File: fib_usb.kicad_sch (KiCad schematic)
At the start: 137 parts, among them J401 USB-C_USB4105-GF-A, J402 Conn_USB-C_WE_632723300011, U402 TPS65988DHRSHR, U403 FT230X_QFN, U404 AP22615A_TSOT26, U405 TUSB1046-DCIRNQ, U406 AP22615A_TSOT26, U407 TPD4E05U06QDQARQ1, U408 TPD4E05U06QDQARQ1, U409 W25Q80DV_USON, U410 TPD4E05U06QDQARQ1, U411 TPD4E05U06QDQARQ1, U412 TPD4E05U06QDQARQ1

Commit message: added some missing footprints, stared working ono power-on and sequencing
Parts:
- U403: footprint jetson-orin-baseboard-footprints:QFN-16-1EP_4x4mm_P0.65mm -> Fibel2:QFN-16_1EP_4x4mm_P0.65mm
- U404, U406: footprint jetson-orin-baseboard-footprints:TSOT23-6 -> Fibel2:TSOT23-6
- U405: footprint jetson-orin-baseboard-footprints:WQFN-40_1EP_6x3mm_Pitch0.4mm_EP4.7x2.7mm -> Fibel2:WQFN-40_1EP_6x3mm_Pitch0.4mm_EP4.7x2.7mm
- U407, U408, U410, U411, U412: footprint jetson-orin-baseboard-footprints:USON-10_2.5x1mm_P0.5mm -> Fibel2:USON-10_2.5x1mm_P0.5mm
- U409: footprint jetson-orin-baseboard-footprints:USON-8_2x3mm_P0.5mm -> Fibel2:USON-8_2x3mm_P0.5mm
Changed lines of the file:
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@@
 			)
 		)
-		(property "Footprint" "jetson-orin-baseboard-footprints:USON-10_2.5x1mm_P0.5mm"
+		(property "Footprint" "Fibel2:USON-10_2.5x1mm_P0.5mm"
 			(at 321.31 160.02 0)
 			(effects
@@
 			)
 		)
-		(property "Footprint" "jetson-orin-baseboard-footprints:TSOT23-6"
+		(property "Footprint" "Fibel2:TSOT23-6"
 			(at 144.78 210.82 0)
 			(effects
@@
 			)
 		)
-		(property "Footprint" "jetson-orin-baseboard-footprints:USON-10_2.5x1mm_P0.5mm"
+		(property "Footprint" "Fibel2:USON-10_2.5x1mm_P0.5mm"
 			(at 346.71 160.02 0)
 			(effects
@@
 			)
 		)
-		(property "Footprint" "jetson-orin-baseboard-footprints:USON-10_2.5x1mm_P0.5mm"
+		(property "Footprint" "Fibel2:USON-10_2.5x1mm_P0.5mm"
 			(at 364.49 220.98 0)
 			(effects
@@
 			)
 		)
-		(property "Footprint" "jetson-orin-baseboard-footprints:USON-10_2.5x1mm_P0.5mm"
+		(property "Footprint" "Fibel2:USON-10_2.5x1mm_P0.5mm"
 			(at 358.14 40.64 0)
 			(effects
@@
 			)
 		)
-		(property "Footprint" "jetson-orin-baseboard-footprints:QFN-16-1EP_4x4mm_P0.65mm"
+		(property "Footprint" "Fibel2:QFN-16_1EP_4x4mm_P0.65mm"
 			(at 96.52 163.83 0)
 			(effects
@@
 			)
 		)
-		(property "Footprint" "jetson-orin-baseboard-footprints:TSOT23-6"
+		(property "Footprint" "Fibel2:TSOT23-6"
 			(at 292.1 55.88 0)
 			(effects
@@
 			)
 		)
-		(property "Footprint" "jetson-orin-baseboard-footprints:USON-10_2.5x1mm_P0.5mm"
+		(property "Footprint" "Fibel2:USON-10_2.5x1mm_P0.5mm"
 			(at 297.18 160.02 0)
 			(effects
@@
 			)
 		)
-		(property "Footprint" "jetson-orin-baseboard-footprints:USON-8_2x3mm_P0.5mm"
+		(property "Footprint" "Fibel2:USON-8_2x3mm_P0.5mm"
 			(at 368.3 185.42 0)
 			(effects
@@
 			)
 		)
-		(property "Footprint" "jetson-orin-baseboard-footprints:WQFN-40_1EP_6x3mm_Pitch0.4mm_EP4.7x2.7mm"
+		(property "Footprint" "Fibel2:WQFN-40_1EP_6x3mm_Pitch0.4mm_EP4.7x2.7mm"
 			(at 251.46 106.68 0)
 			(effects

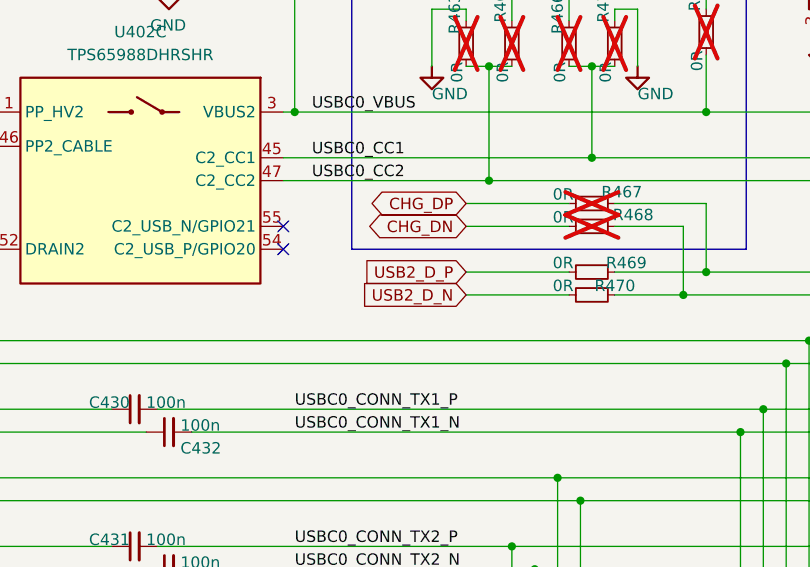
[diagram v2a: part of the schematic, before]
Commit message: started routing the SODIMM, updated connector footprint, started arranging component into sub-areas
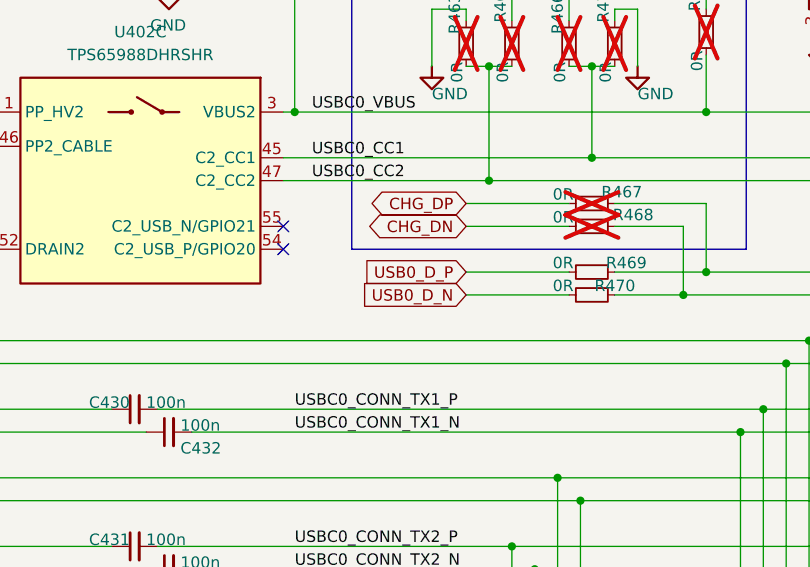
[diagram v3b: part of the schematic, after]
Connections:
- net USB2_D_N renamed USB0_D_N
- net USB2_D_P renamed USB0_D_P
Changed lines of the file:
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@@
 		)
 	)
-	(global_label "USB2_D_N"
+	(global_label "USB0_D_N"
 		(shape input)
 		(at 313.69 93.98 180)
@@
 		)
 	)
-	(global_label "USB2_D_P"
+	(global_label "USB0_D_P"
 		(shape input)
 		(at 313.69 91.44 180)

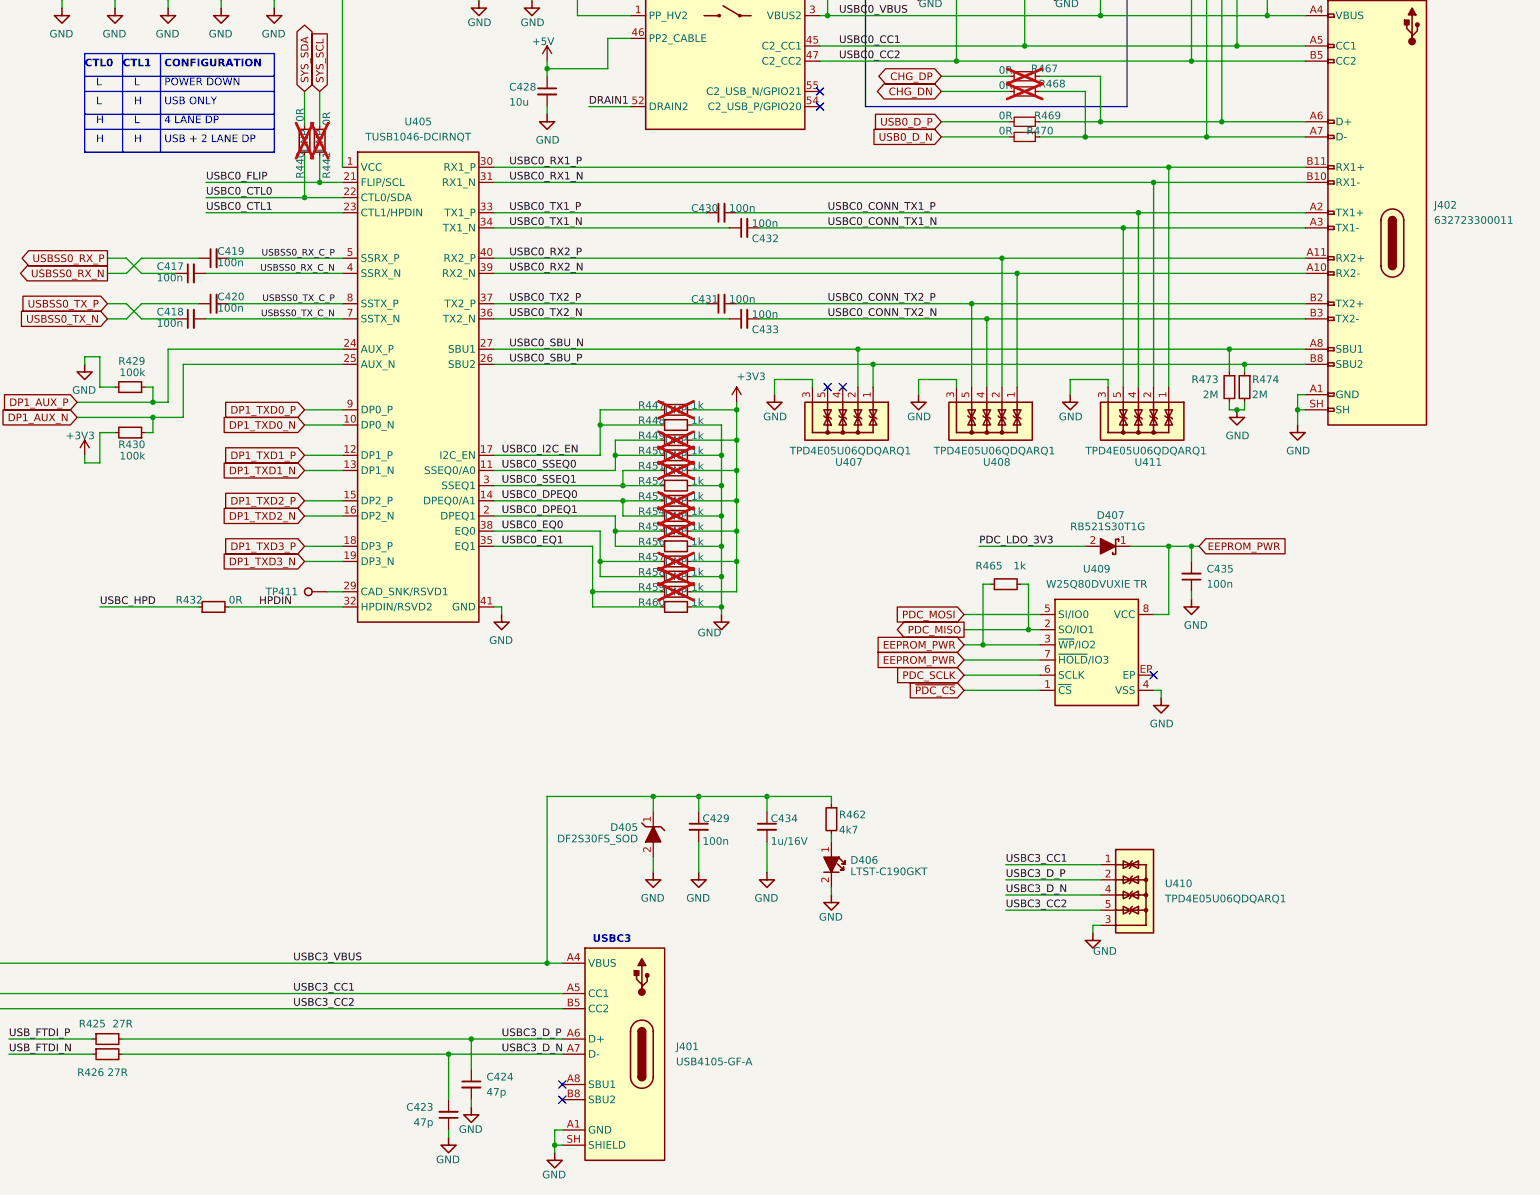
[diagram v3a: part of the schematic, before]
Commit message: did a ton of routing and modeling for SOM, USB, DP & Charging/Power, things starting to take shape
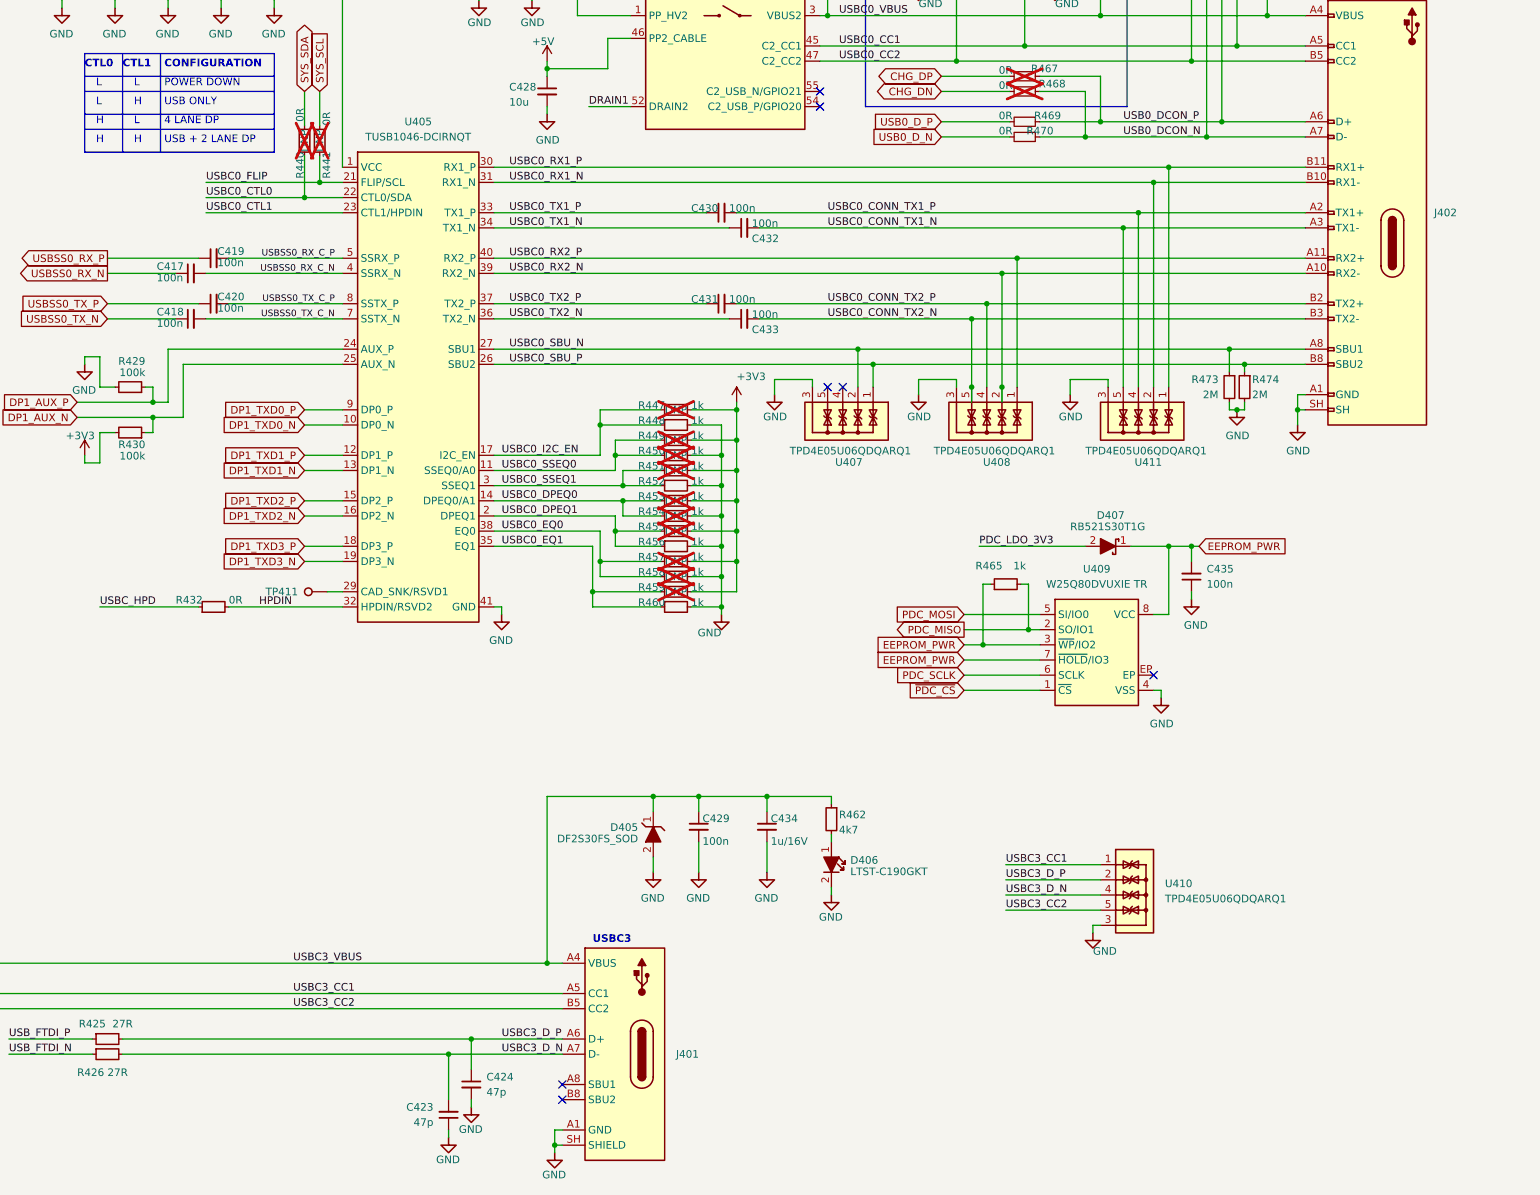
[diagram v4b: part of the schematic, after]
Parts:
- C414, C415, C416, C421: footprint Capacitor_SMD:C_0603_1608Metric -> Capacitor_SMD:C_0402_1005Metric
- C417, C418, C419, C420, C430, C431, C432, C433: footprint Capacitor_SMD:C_0603_1608Metric -> Capacitor_SMD:C_0201_0603Metric
- J401: footprint jetson-orin-baseboard-footprints:USB-C_GCT_USB4105-GF-A -> Fibel2:USB-C_GCT_USB4105-GF-A; symbol jetson-orin-baseboard:USB-C_GCT_USB4105-GF-A -> Fibel2:USB-C_USB4105-GF-A
- J402: footprint jetson-orin-baseboard-footprints:Conn_USB-C_WE_632723300011 -> Fibel2:Conn_USB-C_WE_632723300011; symbol jetson-orin-baseboard:USB-C_WE_632723300011 -> Fibel2:Conn_USB-C_WE_632723300011
- R447, R448, R449, R450, R451, R452, R453, R454, R455, R456, R457, R458, R459, R460, R469, R470: footprint Resistor_SMD:R_0603_1608Metric -> Resistor_SMD:R_0402_1005Metric
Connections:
- net USBC0_CONN_TX2_N: now also U408.5, U408.6; no longer U408.4, U408.7
- net USBC0_CONN_TX2_P: now also U408.4, U408.7; no longer U408.5, U408.6
- net USBC0_RX2_N: now also U408.2, U408.9; no longer U408.1, U408.10
- net USBC0_RX2_P: now also U408.1, U408.10; no longer U408.2, U408.9
- net USBSS0_RX_N: now also C417.1; no longer C419.1
- net USBSS0_RX_P: now also C419.1; no longer C417.1
- net USBSS0_TX_N: now also C418.1; no longer C420.1
- net USBSS0_TX_P: now also C420.1; no longer C418.1
- net USB0_DCON_N: now reaches J402.A7 (D-), J402.B7 (D-), R468.1, R470.1, U412.4, U412.7
- net USB0_DCON_P: now reaches J402.A6 (D+), J402.B6 (D+), R467.1, R469.1, U412.2, U412.9

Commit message: did some work on the  ports and layout
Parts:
- removed U402: TPS65988DHRSHR, Fibel2:IC_TPS65987DDHRSHR, symbol Fibel2:TPS65988DHRSHR
- added U3: TPS65988DHRSHR, Fibel2:IC_TPS65987DDHRSHR, symbol Fibel2:TPS65988DHRSHR
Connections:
- net +3V3: now also U3.5 (VIN_3V3)
- net +5V: now also U3.25 (PP1_CABLE), U3.46 (PP2_CABLE)
- net DRAIN1: now also U3.15 (DRAIN1), U3.19 (DRAIN1), U3.58 (DRAIN1), U3.8 (DRAIN1)
- net DRAIN2: now also U3.52 (DRAIN2), U3.56 (DRAIN2), U3.57 (DRAIN2), U3.7 (DRAIN2)
- net GND: now also U3.20 (GND), U3.51 (GND), U3.59 (GND_EP)
- net PDC_ADCIN1: now also U3.6 (ADCIN1)
- net PDC_ADCIN2: now also U3.10 (ADCIN2)
- net PDC_CTL0: now also U3.17 (GPIO1)
- net PDC_CTL1: now also U3.18 (GPIO2)
- net PDC_FLIP: now also U3.16 (GPIO0)
- net PDC_GPIO14: now also U3.42 (GPIO14/PWM1)
- net PDC_GPIO15: now also U3.43 (GPIO15/PWM2)
- net PDC_HPD2: now also U3.31 (GPIO4/HPD2)
- net PDC_I2C1_IRQn: now also U3.29 (~{I2C1_IRQ})
- net PDC_I2C1_SCL: now also U3.27 (I2C1_SCL)
- net PDC_I2C1_SDA: now also U3.28 (I2C1_SDA)
- net PDC_I2C2_IRQn: now also U3.34 (~{I2C2_IRQ})
- net PDC_I2C2_SCL: now also U3.32 (I2C2_SCL)
- net PDC_I2C2_SDA: now also U3.33 (I2C2_SDA)
- net PDC_I2C3_SCL: now also U3.21 (I2C3_SCL/GPIO5)
- net PDC_I2C3_SDA: now also U3.22 (I2C3_SDA/GPIO6)
- net PDC_LDO_1V8: now also U3.35 (LDO_1V8)
- net PDC_LDO_3V3: now also U3.9 (LDO_3V3)
- net PDC_MISO: now also U3.36 (SPI_POCI/GPIO8)
- net PDC_MOSI: now also U3.37 (SPI_PICO/GPIO9)
- net PDC_RESET: now also U3.44 (HRESET)
- net PDC_SCLK: now also U3.38 (SPI_CLK/GPIO10)
- net USB0_DCON_N: now also U412.5, U412.6; no longer U412.4, U412.7
- net USB0_DCON_P: now also U412.4, U412.7; no longer U412.2, U412.9
- net USBC0_5V_PEN: now also U3.49 (GPIO17/PP_EXT2)
- net USBC0_CC1: now also U3.24 (C1_CC1)
- net USBC0_CC2: now also U412.2, U412.9, U3.26 (C1_CC2); no longer U412.5, U412.6
- net USBC0_VBUS: now also U3.13 (VBUS1)
- net USBC3_5V_PEN: now also U3.48 (GPIO16/PP_EXT1)
- net USBC3_CC1: now also U3.45 (C2_CC1)
- net USBC3_CC2: now also U3.47 (C2_CC2)
- net USBC3_VBUS: now also U3.3 (VBUS2)
- net USBPD1_HV: now also U3.1 (PP_HV2)
- net USBPD2_HV: now also U3.11 (PP_HV1)
- net ~{PDC_CS}: now also U3.39 (~{SPI_CS}/GPIO11)
- net ~{PDC_I2C3_IRQ}: now also U3.23 (~{I2C3_IRQ}/GPIO7)
- net at TP410.1: now also U3.30 (GPIO3/HPD1)
